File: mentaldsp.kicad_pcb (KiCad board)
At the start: 2 copper layers, 125 x 35 mm, 30 parts, among them J5 NEMA Conn, J7 NEMA Conn, J8 NEMA Conn, J9 Barrel_Jack_Switch, U6 ESP32-S3-SUPERMINI, U7 TMC2209_N0, U8 TMC2209_N2, U9 TMC2209_N1

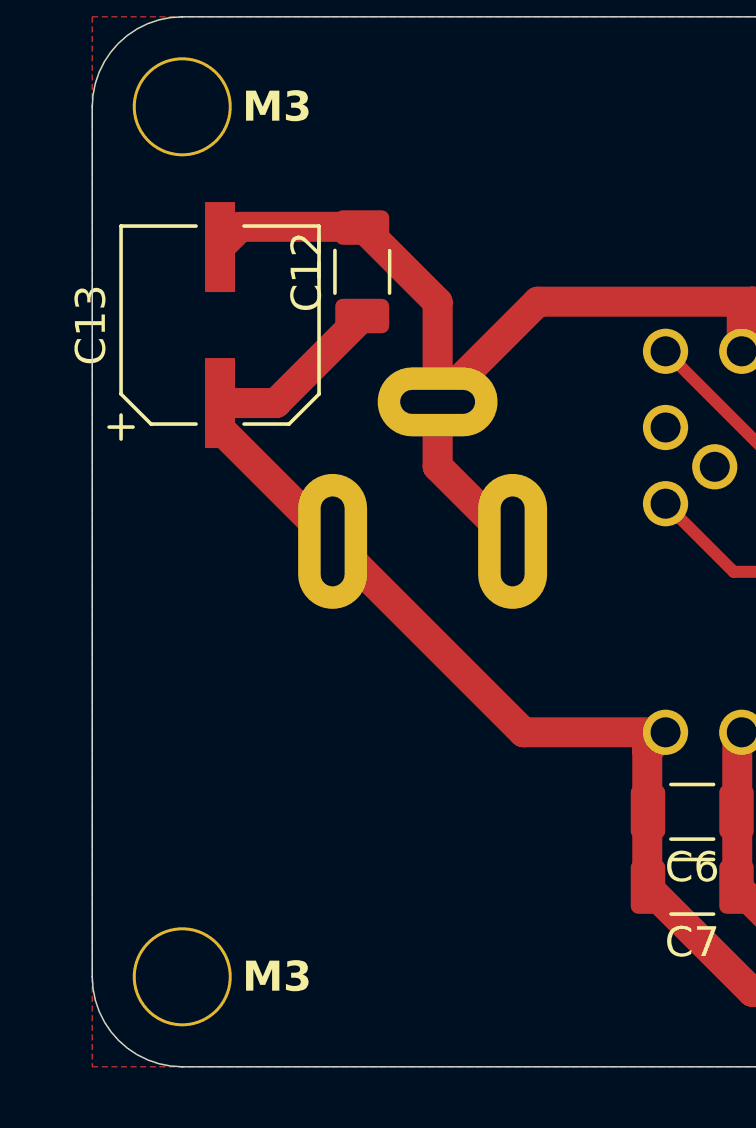
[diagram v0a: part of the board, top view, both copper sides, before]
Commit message: replace to SMD jack
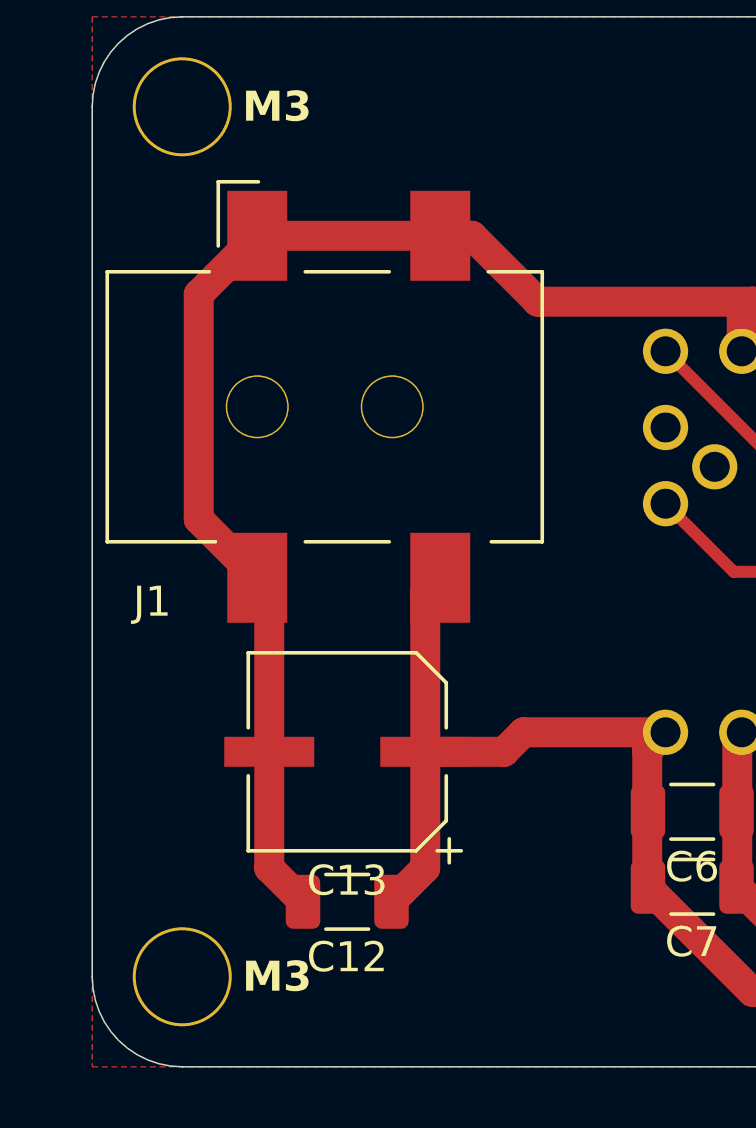
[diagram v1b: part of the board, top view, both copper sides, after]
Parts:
- removed J9: Barrel_Jack_Switch, lib_footprint:Generic_PowerJack
- added J1: Conn_PWRJack_2x5.5mm_CUIDevices_PJ-002AH-SMT-TR, PCM_fab:CUIDevices_PJ-002AH-SMT-TR_PWRJack_2x5.5mm, F.Cu at (108.5, 113.0)
- moved C12 21.0 mm to (108.5, 129.5), turned to 180 degrees
- moved C13 14.8 mm to (108.5, 124.5), turned to 180 degrees
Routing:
- net GND: track 257.8 -> 270.2 mm
- net +12V: track 102.0 -> 96.0 mm

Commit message: fix polarity
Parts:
- moved C13 0.10 mm to (108.4, 124.5)
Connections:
- J1 pad 3: GND -> +12V
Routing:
- net +12V: track 96.0 -> 102.2 mm
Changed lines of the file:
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@@
 			(size 3 2)
 			(layers "F.Cu" "F.Mask" "F.Paste")
-			(net "GND")
+			(net "+12V")
 			(pintype "passive")
 		)
@@
 	(footprint "PCM_fab:CP_Elec_100uF_Panasonic_EEE-FN1E101UL"
 		(layer "F.Cu")
-		(at 108.5 124.5 180)
+		(at 108.4 124.5 180)
 		(descr "SMD capacitor, aluminum electrolytic, Nichicon, 10.0x10.0mm")
 		(tags "capacitor electrolytic")
@@
 	)
 	(segment
-		(start 105.9 124.5)
-		(end 105.9 119.1)
-		(width 1)
-		(layer "F.Cu")
-		(net "GND")
-	)
-	(segment
 		(start 124.19 109.686)
 		(end 124 109.496)
@@
 	)
 	(segment
+		(start 111.6 107.3)
+		(end 112.6565 107.3)
+		(width 1)
+		(layer "F.Cu")
+		(net "GND")
+	)
+	(segment
 		(start 121.65 109.846)
 		(end 122 109.496)
@@
 	)
 	(segment
-		(start 105.9 124.5)
-		(end 105.9 128.375)
+		(start 103.55 109.25)
+		(end 105.5 107.3)
 		(width 1)
 		(layer "F.Cu")
@@
 	)
 	(segment
-		(start 105.5 107.3)
-		(end 103.55 109.25)
-		(width 1)
-		(layer "F.Cu")
-		(net "GND")
-	)
-	(segment
-		(start 103.55 109.25)
-		(end 103.55 116.75)
+		(start 153.66 106)
+		(end 158.81 111.15)
 		(width 1)
 		(layer "F.Cu")
@@
 	)
 	(segment
-		(start 153.66 106)
-		(end 158.81 111.15)
+		(start 121.5 124)
+		(end 121.65 123.85)
 		(width 1)
 		(layer "F.Cu")
@@
 	)
 	(segment
-		(start 121.5 124)
-		(end 121.65 123.85)
+		(start 105.8 124.5)
+		(end 103.55 122.25)
 		(width 1)
 		(layer "F.Cu")
@@
 	)
 	(segment
-		(start 105.5 107.3)
-		(end 111.6 107.3)
+		(start 122 109.496)
+		(end 124 109.496)
 		(width 1)
 		(layer "F.Cu")
@@
 	)
 	(segment
-		(start 122 109.496)
-		(end 124 109.496)
+		(start 175.5 129)
+		(end 175.5 126.5)
 		(width 1)
 		(layer "F.Cu")
@@
 	)
 	(segment
-		(start 175.5 129)
-		(end 175.5 126.5)
+		(start 105.5 107.3)
+		(end 111.6 107.3)
 		(width 1)
 		(layer "F.Cu")
@@
 	)
 	(segment
-		(start 105.9 119.1)
-		(end 105.5 118.7)
-		(width 1)
-		(layer "F.Cu")
-		(net "GND")
-	)
-	(segment
 		(start 148.5 124)
 		(end 148.65 123.85)
@@
 	)
 	(segment
-		(start 112.6565 107.3)
-		(end 114.8525 109.496)
+		(start 103.55 122.25)
+		(end 103.55 109.25)
 		(width 1)
 		(layer "F.Cu")
@@
 	)
 	(segment
+		(start 105.8 124.5)
+		(end 105.8 128.275)
+		(width 1)
+		(layer "F.Cu")
+		(net "GND")
+	)
+	(segment
 		(start 175.65 123.85)
 		(end 173.996 122.196)
@@
 	)
 	(segment
-		(start 111.6 107.3)
-		(end 112.6565 107.3)
-		(width 1)
-		(layer "F.Cu")
-		(net "GND")
-	)
-	(segment
 		(start 173.996 122.196)
 		(end 165.544 122.196)
@@
 	)
 	(segment
-		(start 187.464 112.804)
-		(end 216.996 112.804)
+		(start 112.6565 107.3)
+		(end 114.8525 109.496)
 		(width 1)
 		(layer "F.Cu")
@@
 	)
 	(segment
-		(start 103.55 116.75)
-		(end 105.5 118.7)
+		(start 187.464 112.804)
+		(end 216.996 112.804)
 		(width 1)
 		(layer "F.Cu")
@@
 	)
 	(segment
+		(start 105.8 128.275)
+		(end 107.025 129.5)
+		(width 1)
+		(layer "F.Cu")
+		(net "GND")
+	)
+	(segment
 		(start 165.544 122.196)
 		(end 163.89 123.85)
@@
 	)
 	(segment
-		(start 105.9 128.375)
-		(end 107.025 129.5)
-		(width 1)
-		(layer "F.Cu")
-		(net "GND")
-	)
-	(segment
 		(start 124.19 111.15)
 		(end 124.19 109.686)
@@
 	)
 	(segment
-		(start 111.1 124.5)
-		(end 113.7265 124.5)
+		(start 111 124.5)
+		(end 118.46 124.5)
 		(width 1)
 		(layer "F.Cu")
@@
 	)
 	(segment
-		(start 113.7265 124.5)
-		(end 114.3765 123.85)
+		(start 118.46 124.5)
+		(end 119.11 123.85)
 		(width 1)
 		(layer "F.Cu")
@@
 	)
 	(segment
+		(start 111 128.475)
+		(end 109.975 129.5)
+		(width 1)
+		(layer "F.Cu")
+		(net "+12V")
+	)
+	(segment
 		(start 143.1525 132.5)
 		(end 122 132.5)
@@
 	)
 	(segment
-		(start 172.5 124.46)
-		(end 173.11 123.85)
+		(start 111.6 118.7)
+		(end 111.6 123.9)
 		(width 1)
 		(layer "F.Cu")
@@
 	)
 	(segment
-		(start 145.5 124.46)
-		(end 146.11 123.85)
+		(start 105.5 118.7)
+		(end 111.6 118.7)
 		(width 1)
 		(layer "F.Cu")
@@
 	)
 	(segment
-		(start 111.1 128.375)
-		(end 109.975 129.5)
+		(start 172.5 124.46)
+		(end 173.11 123.85)
 		(width 1)
 		(layer "F.Cu")
@@
 	)
 	(segment
-		(start 111.1 124.5)
-		(end 111.1 119.2)
+		(start 145.5 124.46)
+		(end 146.11 123.85)
 		(width 1)
 		(layer "F.Cu")
@@
 	)
 	(segment
-		(start 111.1 119.2)
-		(end 111.6 118.7)
-		(width 1)
-		(layer "F.Cu")
-		(net "+12V")
-	)
-	(segment
-		(start 114.3765 123.85)
-		(end 119.11 123.85)
+		(start 111.6 123.9)
+		(end 111 124.5)
 		(width 1)
 		(layer "F.Cu")
@@
 	)
 	(segment
-		(start 111.1 124.5)
-		(end 111.1 128.375)
-		(width 1)
-		(layer "F.Cu")
-		(net "+12V")
-	)
-	(segment
 		(start 118.5 129)
 		(end 118.5 126.5)
@@
 		(width 1)
 		(layer "F.Cu")
+		(net "+12V")
+	)
+	(segment
+		(start 111 124.5)
+		(end 111 128.475)
+		(width 1)
+		(layer "F.Cu")

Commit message: housekeeping
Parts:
- moved R2 19.3 mm to (200.8, 108.1)
- moved C13 19.3 mm to (93.4, 112.3)
- moved C1 19.3 mm to (120.5, 114.3)
- moved C10 19.3 mm to (159.0, 114.3)
- moved C11 19.3 mm to (159.0, 116.8)
- moved C12 19.3 mm to (93.5, 117.3)
- moved C2 19.3 mm to (147.5, 114.3)
- moved C3 19.3 mm to (174.5, 114.3)
- moved C4 19.3 mm to (202.0, 102.1)
- moved C5 19.3 mm to (204.5, 102.1)
- moved C6 19.3 mm to (105.0, 114.3)
- moved C7 19.3 mm to (105.0, 116.8)
- moved C8 19.3 mm to (132.0, 114.3)
- moved C9 19.3 mm to (132.0, 116.8)
- moved H1 19.3 mm to (207.0, 119.8)
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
